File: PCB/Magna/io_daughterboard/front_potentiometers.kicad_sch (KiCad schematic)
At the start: 33 parts

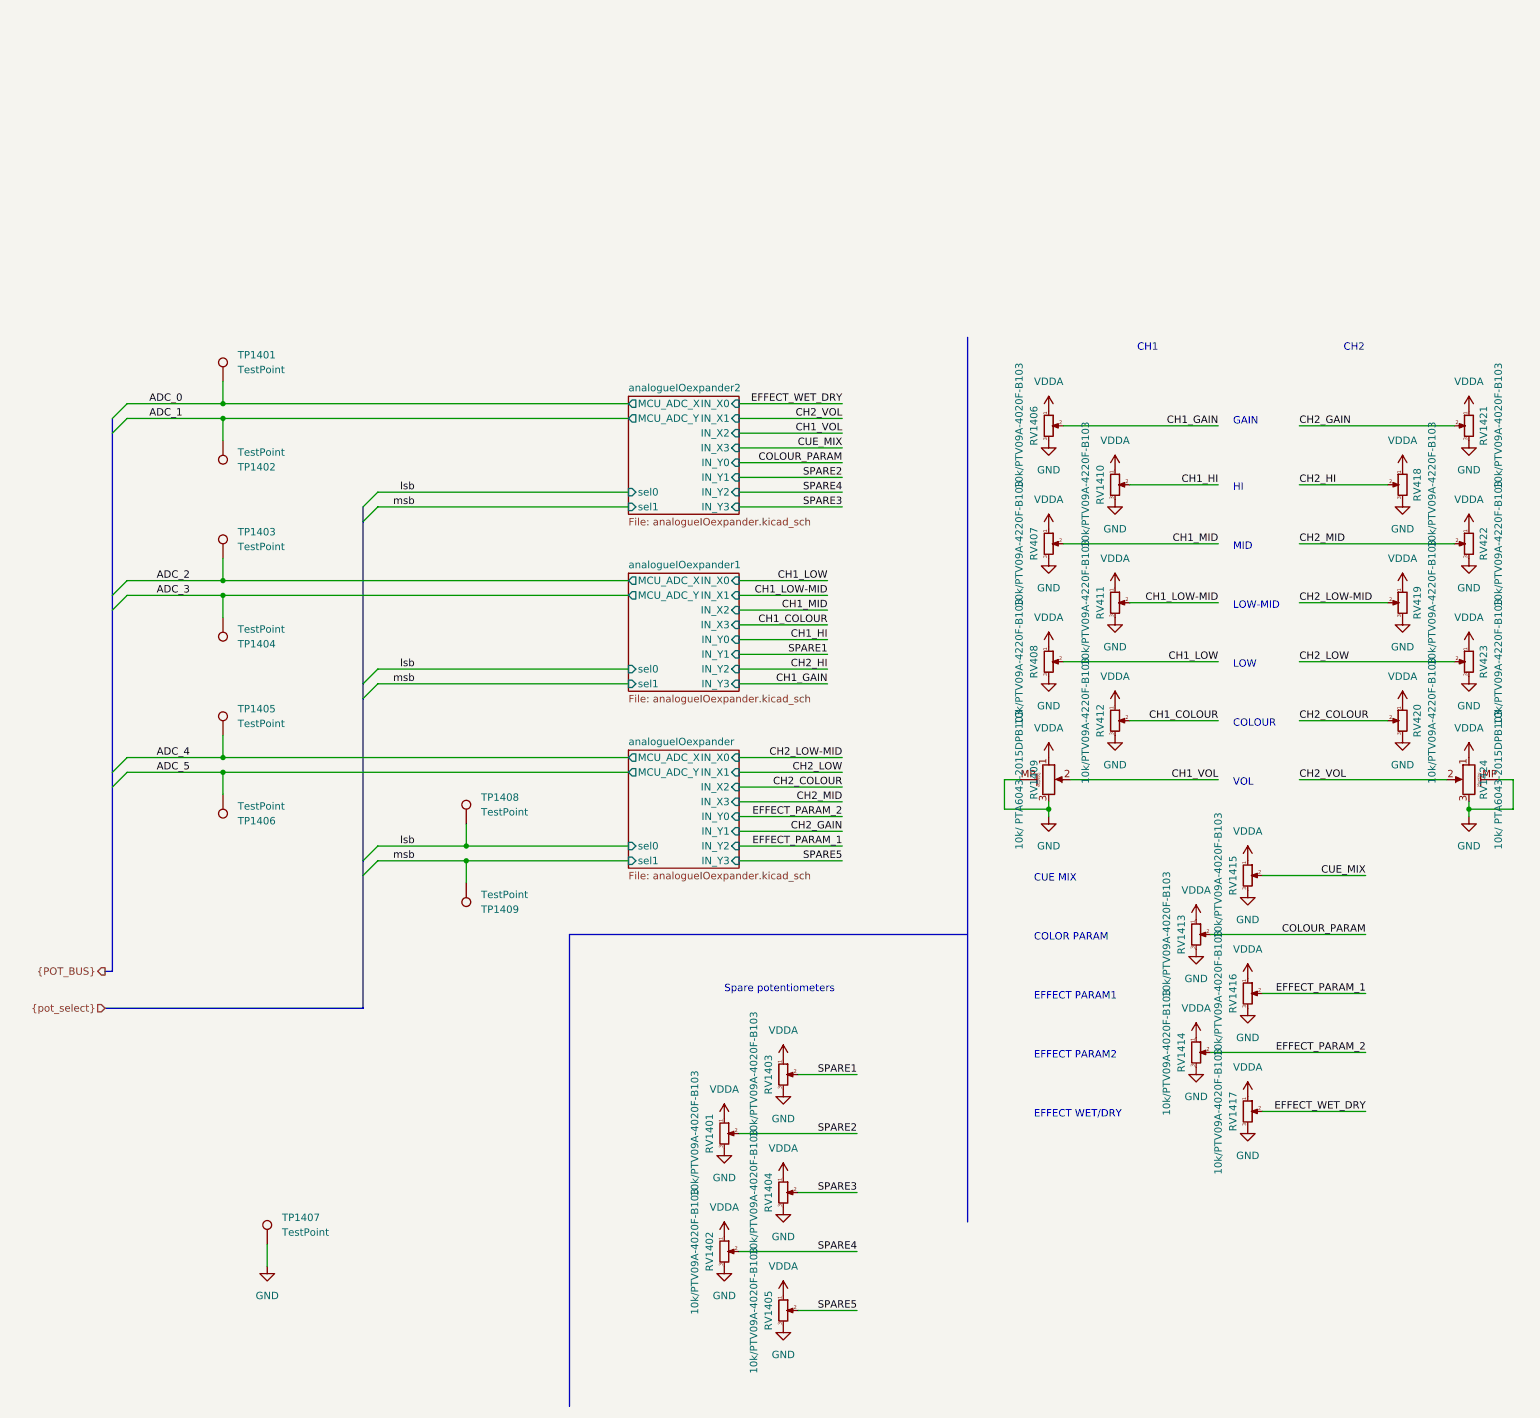
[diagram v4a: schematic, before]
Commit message: Change Cue Mix potentiometer to front facing model
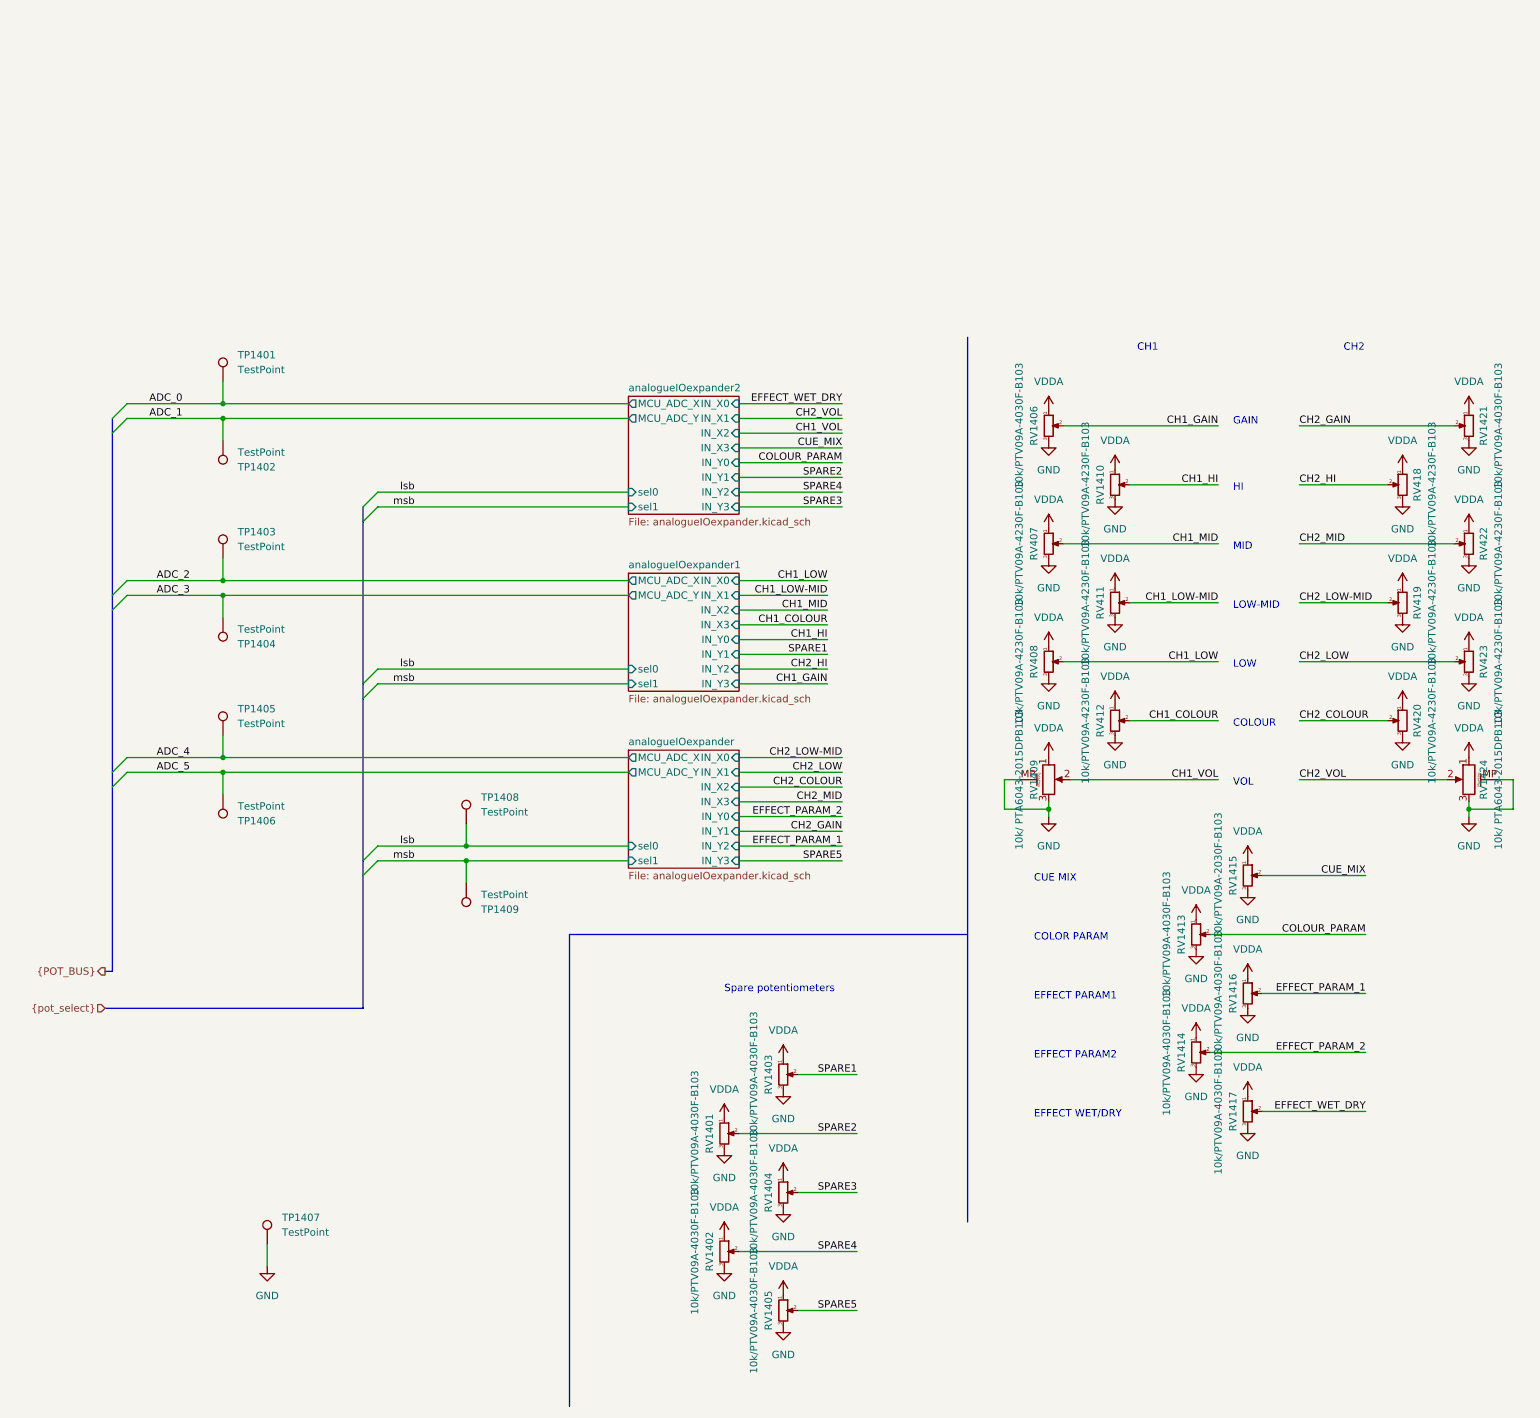
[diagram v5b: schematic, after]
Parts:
- RV1401, RV1402, RV1403, RV1404, RV1405, RV1406, RV1413, RV1414, RV1416, RV1417, RV1421: value 10k/PTV09A-4020F-B103 -> 10k/PTV09A-4030F-B103
- RV1410, RV407, RV408, RV411, RV412, RV418, RV419, RV420, RV422, RV423: value 10k/PTV09A-4220F-B103 -> 10k/PTV09A-4230F-B103
- RV1415: value 10k/PTV09A-4020F-B103 -> 10k/PTV09A-2030F-B103; footprint Potentiometer_THT:Potentiometer_Bourns_PTV09A-1_Single_Vertical -> Potentiometer_THT:Potentiometer_Bourns_PTV09A-2_Single_Horizontal
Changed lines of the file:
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@@
       (effects (font (size 1.27 1.27)))
     )
-    (property "Value" "10k/PTV09A-4020F-B103 " (at 220.98 105.41 90)
-      (effects (font (size 1.27 1.27)))
-    )
-    (property "Footprint" "Potentiometer_THT:Potentiometer_Bourns_PTV09A-1_Single_Vertical" (at 226.06 105.41 0)
+    (property "Value" "10k/PTV09A-2030F-B103" (at 220.98 105.41 90)
+      (effects (font (size 1.27 1.27)))
+    )
+    (property "Footprint" "Potentiometer_THT:Potentiometer_Bourns_PTV09A-2_Single_Horizontal" (at 226.06 105.41 0)
       (effects (font (size 1.27 1.27)) hide)
     )
@@
       (effects (font (size 1.27 1.27)))
     )
-    (property "Value" "10k/PTV09A-4020F-B103 " (at 130.81 149.86 90)
+    (property "Value" "10k/PTV09A-4030F-B103 " (at 130.81 149.86 90)
       (effects (font (size 1.27 1.27)))
     )
@@
       (effects (font (size 1.27 1.27)))
     )
-    (property "Value" "10k/PTV09A-4020F-B103 " (at 140.97 180.34 90)
+    (property "Value" "10k/PTV09A-4030F-B103 " (at 140.97 180.34 90)
       (effects (font (size 1.27 1.27)))
     )
@@
       (effects (font (size 1.27 1.27)))
     )
-    (property "Value" "10k/PTV09A-4020F-B103 " (at 220.98 146.05 90)
+    (property "Value" "10k/PTV09A-4030F-B103 " (at 220.98 146.05 90)
       (effects (font (size 1.27 1.27)))
     )
@@
       (effects (font (size 1.27 1.27)))
     )
-    (property "Value" "10k/PTV09A-4220F-B103 " (at 186.69 48.26 90)
+    (property "Value" "10k/PTV09A-4230F-B103 " (at 186.69 48.26 90)
       (effects (font (size 1.27 1.27)))
     )
@@
       (effects (font (size 1.27 1.27)))
     )
-    (property "Value" "10k/PTV09A-4020F-B103 " (at 212.09 135.89 90)
+    (property "Value" "10k/PTV09A-4030F-B103 " (at 212.09 135.89 90)
       (effects (font (size 1.27 1.27)))
     )
@@
       (effects (font (size 1.27 1.27)))
     )
-    (property "Value" "10k/PTV09A-4220F-B103 " (at 257.81 58.42 90)
+    (property "Value" "10k/PTV09A-4230F-B103 " (at 257.81 58.42 90)
       (effects (font (size 1.27 1.27)))
     )
@@
       (effects (font (size 1.27 1.27)))
     )
-    (property "Value" "10k/PTV09A-4220F-B103 " (at 269.24 68.58 90)
+    (property "Value" "10k/PTV09A-4230F-B103 " (at 269.24 68.58 90)
       (effects (font (size 1.27 1.27)))
     )
@@
       (effects (font (size 1.27 1.27)))
     )
-    (property "Value" "10k/PTV09A-4220F-B103 " (at 198.12 38.1 90)
+    (property "Value" "10k/PTV09A-4230F-B103 " (at 198.12 38.1 90)
       (effects (font (size 1.27 1.27)))
     )
@@
       (effects (font (size 1.27 1.27)))
     )
-    (property "Value" "10k/PTV09A-4220F-B103 " (at 257.81 78.74 90)
+    (property "Value" "10k/PTV09A-4230F-B103 " (at 257.81 78.74 90)
       (effects (font (size 1.27 1.27)))
     )
@@
       (effects (font (size 1.27 1.27)))
     )
-    (property "Value" "10k/PTV09A-4220F-B103 " (at 186.69 68.58 90)
+    (property "Value" "10k/PTV09A-4230F-B103 " (at 186.69 68.58 90)
       (effects (font (size 1.27 1.27)))
     )
@@
       (effects (font (size 1.27 1.27)))
     )
-    (property "Value" "10k/PTV09A-4020F-B103 " (at 140.97 139.7 90)
+    (property "Value" "10k/PTV09A-4030F-B103 " (at 140.97 139.7 90)
       (effects (font (size 1.27 1.27)))
     )
@@
       (effects (font (size 1.27 1.27)))
     )
-    (property "Value" "10k/PTV09A-4220F-B103 " (at 269.24 48.26 90)
+    (property "Value" "10k/PTV09A-4230F-B103 " (at 269.24 48.26 90)
       (effects (font (size 1.27 1.27)))
     )
@@
       (effects (font (size 1.27 1.27)))
     )
-    (property "Value" "10k/PTV09A-4020F-B103 " (at 269.24 27.94 90)
+    (property "Value" "10k/PTV09A-4030F-B103 " (at 269.24 27.94 90)
       (effects (font (size 1.27 1.27)))
     )
@@
       (effects (font (size 1.27 1.27)))
     )
-    (property "Value" "10k/PTV09A-4020F-B103 " (at 186.69 27.94 90)
+    (property "Value" "10k/PTV09A-4030F-B103 " (at 186.69 27.94 90)
       (effects (font (size 1.27 1.27)))
     )
@@
       (effects (font (size 1.27 1.27)))
     )
-    (property "Value" "10k/PTV09A-4220F-B103 " (at 198.12 78.74 90)
+    (property "Value" "10k/PTV09A-4230F-B103 " (at 198.12 78.74 90)
       (effects (font (size 1.27 1.27)))
     )
@@
       (effects (font (size 1.27 1.27)))
     )
-    (property "Value" "10k/PTV09A-4020F-B103 " (at 130.81 170.18 90)
+    (property "Value" "10k/PTV09A-4030F-B103 " (at 130.81 170.18 90)
       (effects (font (size 1.27 1.27)))
     )
@@
       (effects (font (size 1.27 1.27)))
     )
-    (property "Value" "10k/PTV09A-4220F-B103 " (at 257.81 38.1 90)
+    (property "Value" "10k/PTV09A-4230F-B103 " (at 257.81 38.1 90)
       (effects (font (size 1.27 1.27)))
     )
@@
       (effects (font (size 1.27 1.27)))
     )
-    (property "Value" "10k/PTV09A-4220F-B103 " (at 198.12 58.42 90)
+    (property "Value" "10k/PTV09A-4230F-B103 " (at 198.12 58.42 90)
       (effects (font (size 1.27 1.27)))
     )
@@
       (effects (font (size 1.27 1.27)))
     )
-    (property "Value" "10k/PTV09A-4020F-B103 " (at 212.09 115.57 90)
+    (property "Value" "10k/PTV09A-4030F-B103 " (at 212.09 115.57 90)
       (effects (font (size 1.27 1.27)))
     )
@@
       (effects (font (size 1.27 1.27)))
     )
-    (property "Value" "10k/PTV09A-4020F-B103 " (at 220.98 125.73 90)
+    (property "Value" "10k/PTV09A-4030F-B103 " (at 220.98 125.73 90)
       (effects (font (size 1.27 1.27)))
     )
@@
       (effects (font (size 1.27 1.27)))
     )
-    (property "Value" "10k/PTV09A-4020F-B103 " (at 140.97 160.02 90)
-      (effects (font (size 1.27 1.27)))
-    )
+    (property "Value" "10k/PTV09A-4030F-B103 " (at 140.97 160.02 90)
+      (effects (font (size 1.27 1.27)))
+    )

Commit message: Update some files to KiCad8 and make ready for production
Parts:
- RV1401, RV1402, RV1403, RV1404, RV1405, RV1406, RV1413, RV1414, RV1416, RV1417, RV1421: value 10k/PTV09A-4030F-B103 -> 10k/PTV09A-4030F-B103
- RV1409, RV1424: value 10k/ PTA6043-2015DPB103 -> 10k/ PTA6043-2015DPB103
- RV1410, RV407, RV408, RV411, RV412, RV418, RV419, RV420, RV422, RV423: value 10k/PTV09A-4230F-B103 -> 10k/PTV09A-4230F-B103

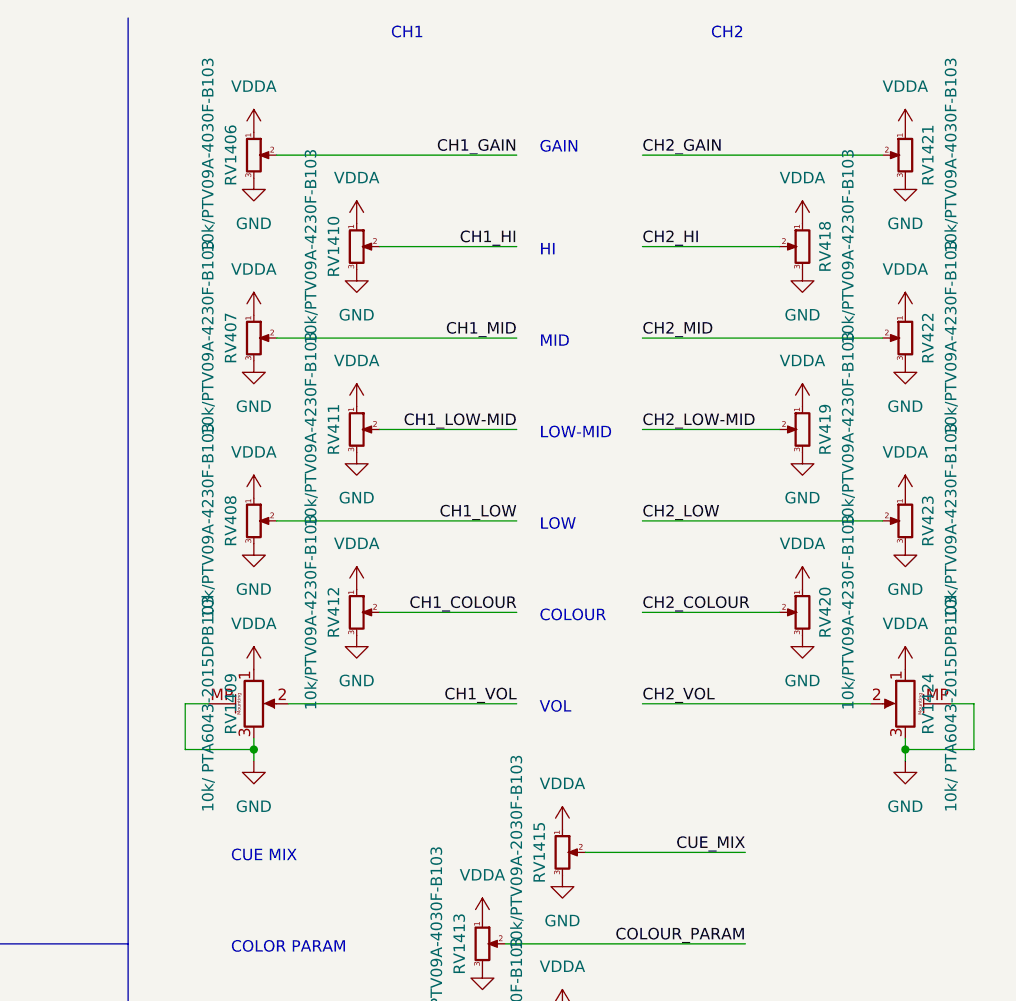
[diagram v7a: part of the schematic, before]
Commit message: Fix some more small issues on IO board
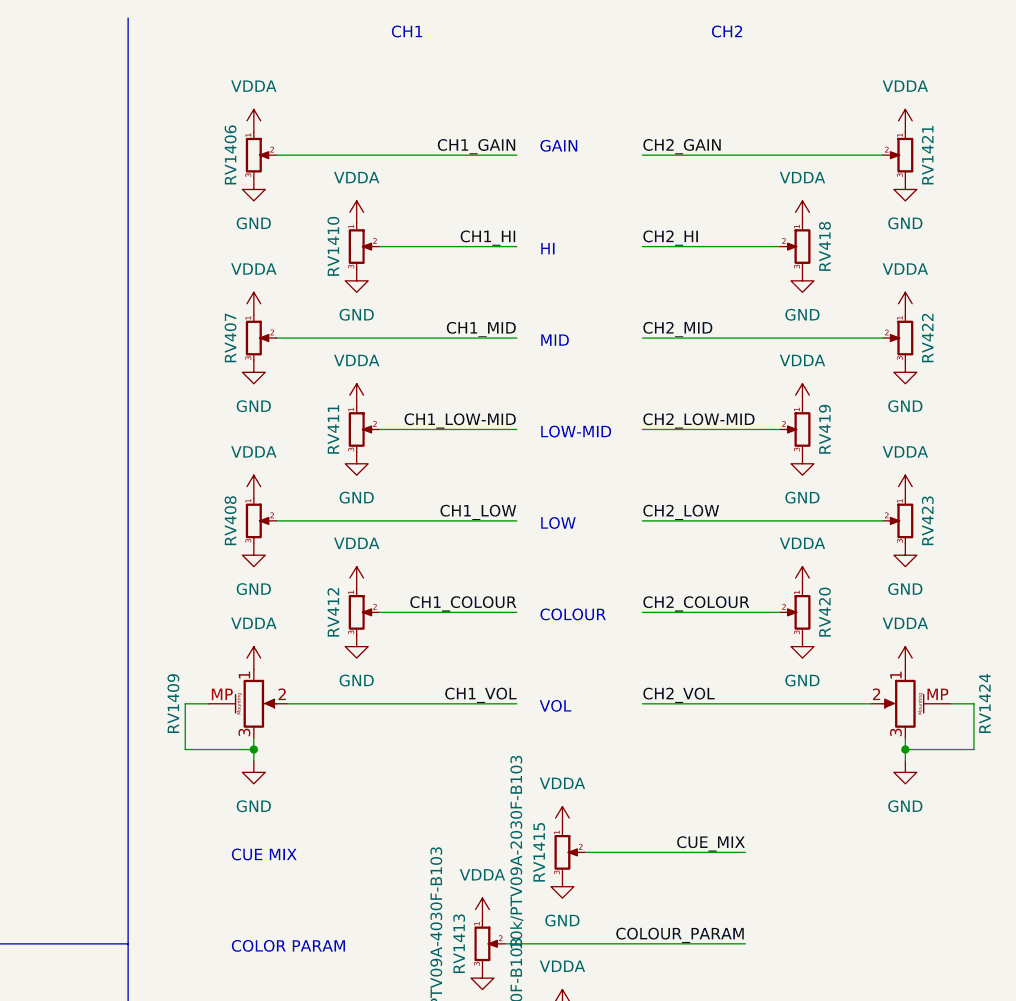
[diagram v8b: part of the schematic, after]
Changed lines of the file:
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@@
 					(size 1.27 1.27)
 				)
+				(hide yes)
 			)
 		)
@@
 					(size 1.27 1.27)
 				)
+				(hide yes)
 			)
 		)
@@
 					(size 1.27 1.27)
 				)
+				(hide yes)
 			)
 		)
@@
 					(size 1.27 1.27)
 				)
+				(hide yes)
 			)
 		)
@@
 					(size 1.27 1.27)
 				)
+				(hide yes)
 			)
 		)
@@
 					(size 1.27 1.27)
 				)
+				(hide yes)
 			)
 		)
@@
 					(size 1.27 1.27)
 				)
+				(hide yes)
 			)
 		)
@@
 					(size 1.27 1.27)
 				)
+				(hide yes)
 			)
 		)
@@
 					(size 1.27 1.27)
 				)
+				(hide yes)
 			)
 		)
@@
 					(size 1.27 1.27)
 				)
+				(hide yes)
 			)
 		)
@@
 					(size 1.27 1.27)
 				)
+				(hide yes)
 			)
 		)
@@
 					(size 1.27 1.27)
 				)
+				(hide yes)
 			)
 		)
@@
 		(dnp no)
 		(property "Reference" "RV1424"
-			(at 266.7 88.9 90)
+			(at 273.05 88.9 90)
 			(effects
 				(font
@@
 					(size 1.27 1.27)
 				)
+				(hide yes)
 			)
 		)
@@
 		(dnp no)
 		(property "Reference" "RV1409"
-			(at 189.23 88.9 90)
+			(at 182.88 88.9 90)
 			(effects
 				(font
@@
 					(size 1.27 1.27)
 				)
+				(hide yes)
 			)
 		)
